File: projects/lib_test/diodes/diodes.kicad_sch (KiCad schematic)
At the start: 12 parts

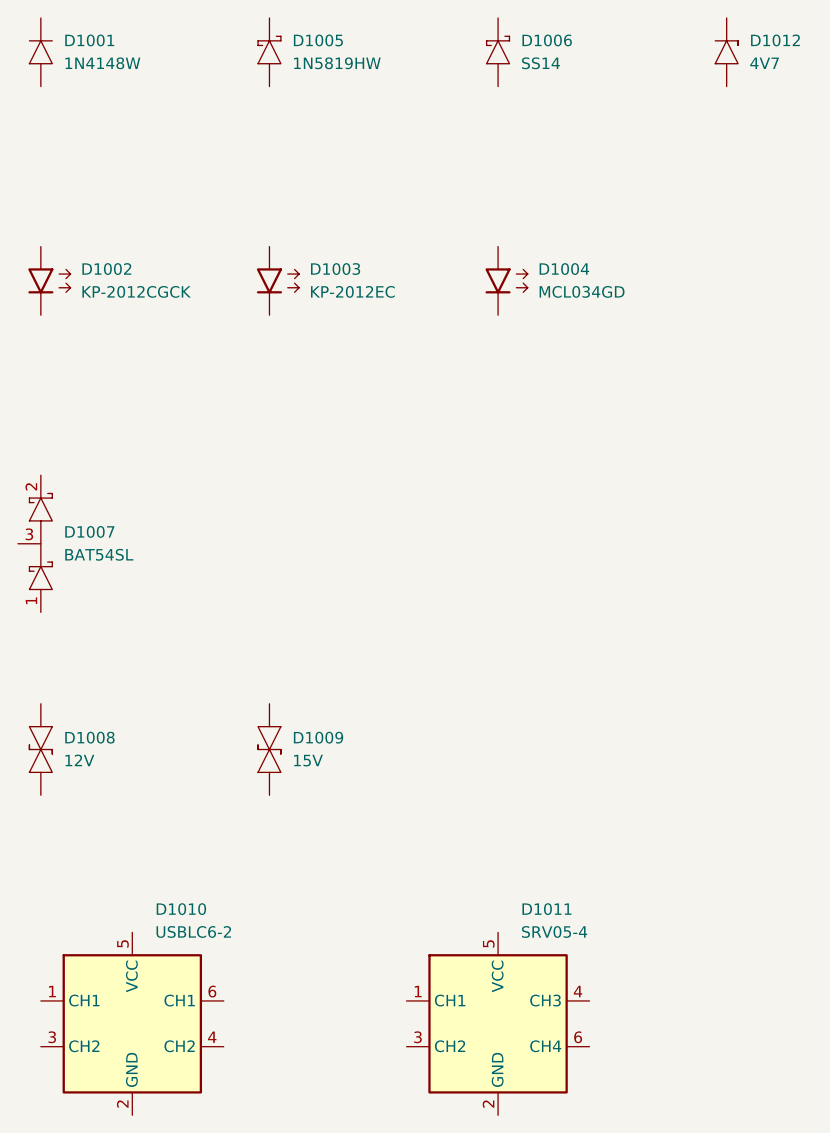
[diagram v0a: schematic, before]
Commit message: update diodes test project
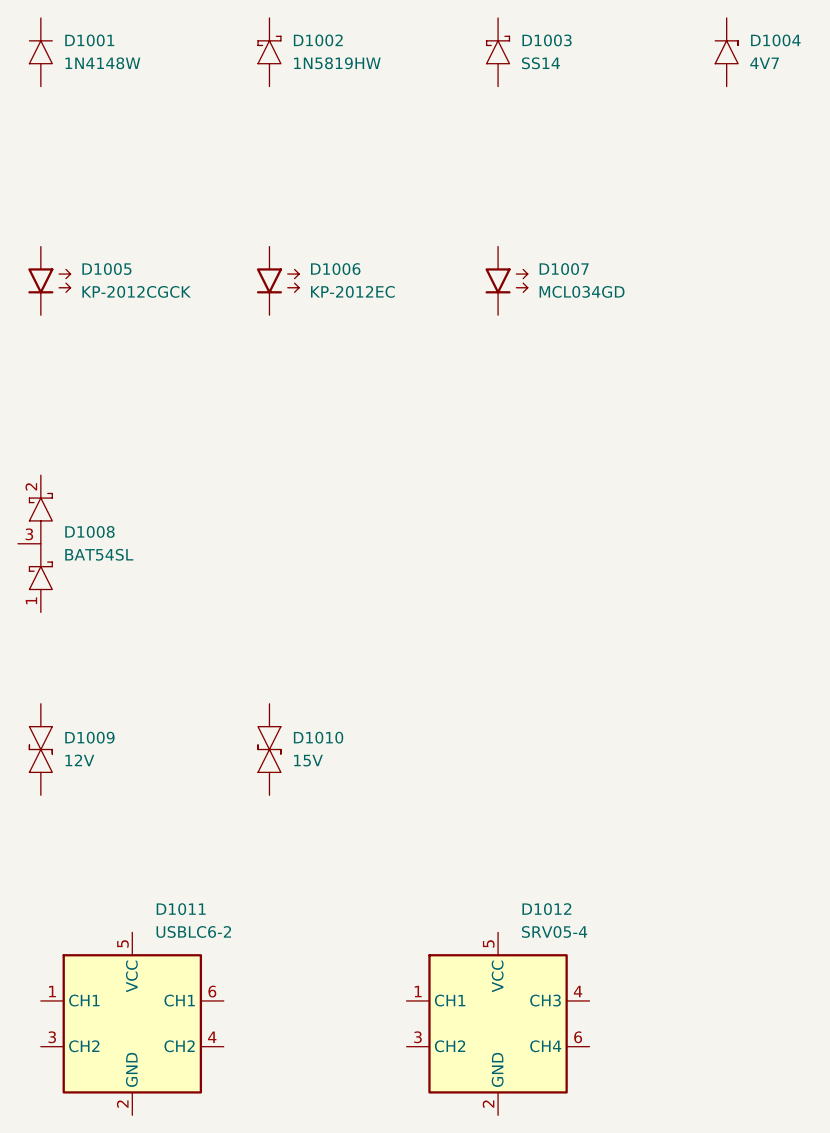
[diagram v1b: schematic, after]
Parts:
- renumbered D1005 to D1002, D1006 to D1003, D1012 to D1004, D1002 to D1005, D1003 to D1006, D1004 to D1007, D1007 to D1008, D1008 to D1009, D1009 to D1010, D1010 to D1011, D1011 to D1012
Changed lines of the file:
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@@
 	(title_block
 		(title "Diodes")
-		(date "2026-01-06")
+		(date "2026-01-09")
 		(rev "1")
 		(comment 1 "-")
@@
 		(on_board yes)
 		(dnp no)
-		(property "Reference" "D1006"
+		(property "Reference" "D1003"
 			(at 78.74 27.94 0)
 			(effects
@@
 			(project ""
 				(path "/e63e39d7-6ac0-4ffd-8aa3-1841a4541b55"
-					(reference "D1006")
+					(reference "D1003")
 					(unit 1)
 				)
@@
 		(on_board yes)
 		(dnp no)
-		(property "Reference" "D1012"
+		(property "Reference" "D1004"
 			(at 104.14 27.94 0)
 			(effects
@@
 			(project ""
 				(path "/e63e39d7-6ac0-4ffd-8aa3-1841a4541b55"
-					(reference "D1012")
+					(reference "D1004")
 					(unit 1)
 				)
@@
 		(on_board yes)
 		(dnp no)
-		(property "Reference" "D1009"
+		(property "Reference" "D1010"
 			(at 53.34 105.41 0)
 			(effects
@@
 			(project ""
 				(path "/e63e39d7-6ac0-4ffd-8aa3-1841a4541b55"
-					(reference "D1009")
+					(reference "D1010")
 					(unit 1)
 				)
@@
 		(on_board yes)
 		(dnp no)
-		(property "Reference" "D1002"
+		(property "Reference" "D1005"
 			(at 29.845 53.34 0)
 			(effects
@@
 			(project ""
 				(path "/e63e39d7-6ac0-4ffd-8aa3-1841a4541b55"
-					(reference "D1002")
+					(reference "D1005")
 					(unit 1)
 				)
@@
 		(on_board yes)
 		(dnp no)
-		(property "Reference" "D1005"
+		(property "Reference" "D1002"
 			(at 53.34 27.94 0)
 			(effects
@@
 			(project ""
 				(path "/e63e39d7-6ac0-4ffd-8aa3-1841a4541b55"
-					(reference "D1005")
+					(reference "D1002")
 					(unit 1)
 				)
@@
 		(on_board yes)
 		(dnp no)
-		(property "Reference" "D1008"
+		(property "Reference" "D1009"
 			(at 27.94 105.41 0)
 			(effects
@@
 			(project ""
 				(path "/e63e39d7-6ac0-4ffd-8aa3-1841a4541b55"
-					(reference "D1008")
+					(reference "D1009")
 					(unit 1)
 				)
@@
 		(on_board yes)
 		(dnp no)
-		(property "Reference" "D1004"
+		(property "Reference" "D1007"
 			(at 80.645 53.34 0)
 			(effects
@@
 			(project ""
 				(path "/e63e39d7-6ac0-4ffd-8aa3-1841a4541b55"
-					(reference "D1004")
+					(reference "D1007")
 					(unit 1)
 				)
@@
 		(on_board yes)
 		(dnp no)
-		(property "Reference" "D1010"
+		(property "Reference" "D1011"
 			(at 38.1 124.46 0)
 			(effects
@@
 			(project ""
 				(path "/e63e39d7-6ac0-4ffd-8aa3-1841a4541b55"
-					(reference "D1010")
+					(reference "D1011")
 					(unit 1)
 				)
@@
 		(on_board yes)
 		(dnp no)
-		(property "Reference" "D1007"
+		(property "Reference" "D1008"
 			(at 27.94 82.55 0)
 			(effects
@@
 			(project ""
 				(path "/e63e39d7-6ac0-4ffd-8aa3-1841a4541b55"
-					(reference "D1007")
+					(reference "D1008")
 					(unit 1)
 				)
@@
 		(on_board yes)
 		(dnp no)
-		(property "Reference" "D1011"
+		(property "Reference" "D1012"
 			(at 78.74 124.46 0)
 			(effects
@@
 			(project ""
 				(path "/e63e39d7-6ac0-4ffd-8aa3-1841a4541b55"
-					(reference "D1011")
+					(reference "D1012")
 					(unit 1)
 				)
@@
 		(on_board yes)
 		(dnp no)
-		(property "Reference" "D1003"
+		(property "Reference" "D1006"
 			(at 55.245 53.34 0)
 			(effects
@@
 			(project ""
 				(path "/e63e39d7-6ac0-4ffd-8aa3-1841a4541b55"
-					(reference "D1003")
+					(reference "D1006")
 					(unit 1)
 				)
